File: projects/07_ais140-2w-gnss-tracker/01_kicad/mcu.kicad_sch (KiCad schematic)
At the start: 22 parts, among them J3 USB-C, J4 DEBUG TC2050, SW1 RESET, SW2 BOOT, U10 W25Q128JV, U8 ESP32-S3-WROOM-1-N8R2, U9 USBLC6-2SC6

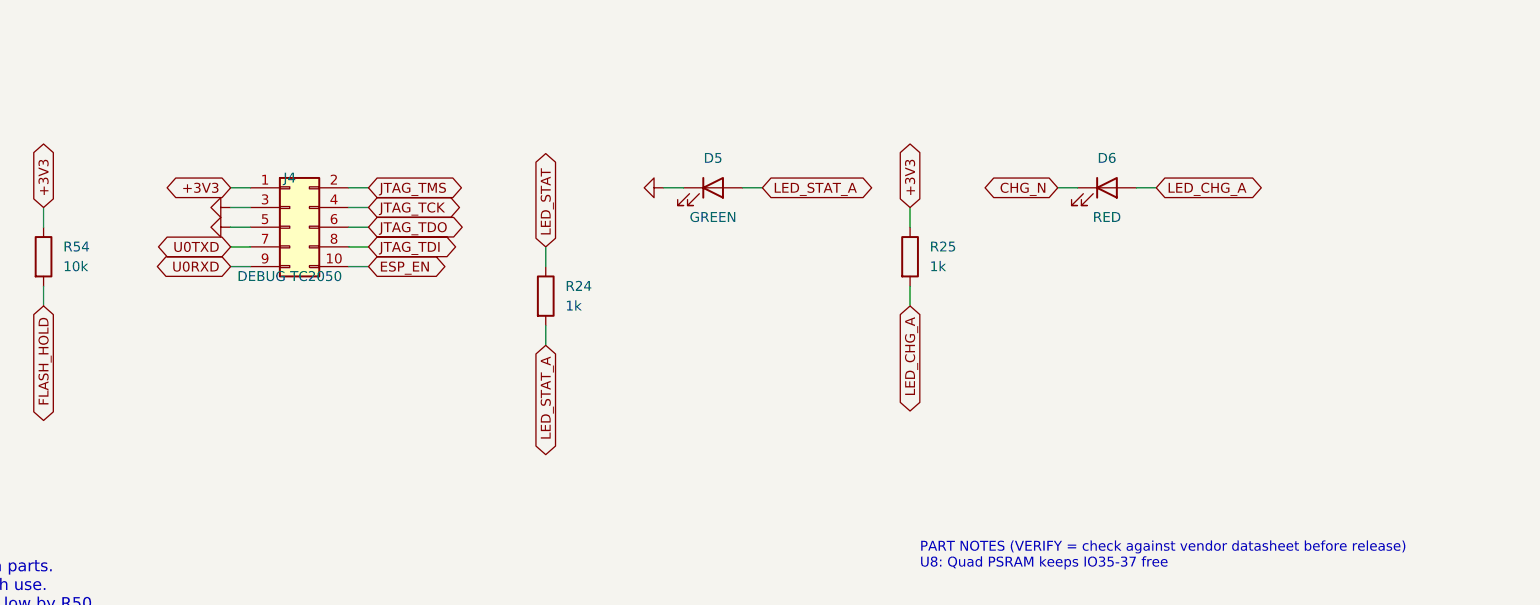
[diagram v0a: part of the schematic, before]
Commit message: Project 07: routed 4-layer PCB, fab outputs and 3D for the AIS-140 tracker
- 60x45 mm 4-layer board, double-sided assembly: KiCad DRC 0 errors / 0 unconnected,
  schematic parity clean, ERC clean
- Flow: anchors + greedy placer, GND/+3V3 fan-out, Freerouting 1.9, grid A* finisher
  with rip-up, RF via fences, edge/area stitching, island vias
- Gerbers + drill (zip), JLC BOM/CPL, engineering BOM, assembly PDFs, STEP + renders
  (envelope models for parts without a KiCad 3D model)
- Programming/JTAG via pogo test pads TP21-TP28 + native USB; R12 removed (TMR open)
- Design report updated with layout summary; DRC/ERC report added

Co-Authored-By: Claude Opus 5.5 <noreply@anthropic.com>
Claude-Session: https://claude.ai/code/session_01Hk6s8R6up8HYVQWXd3atVk
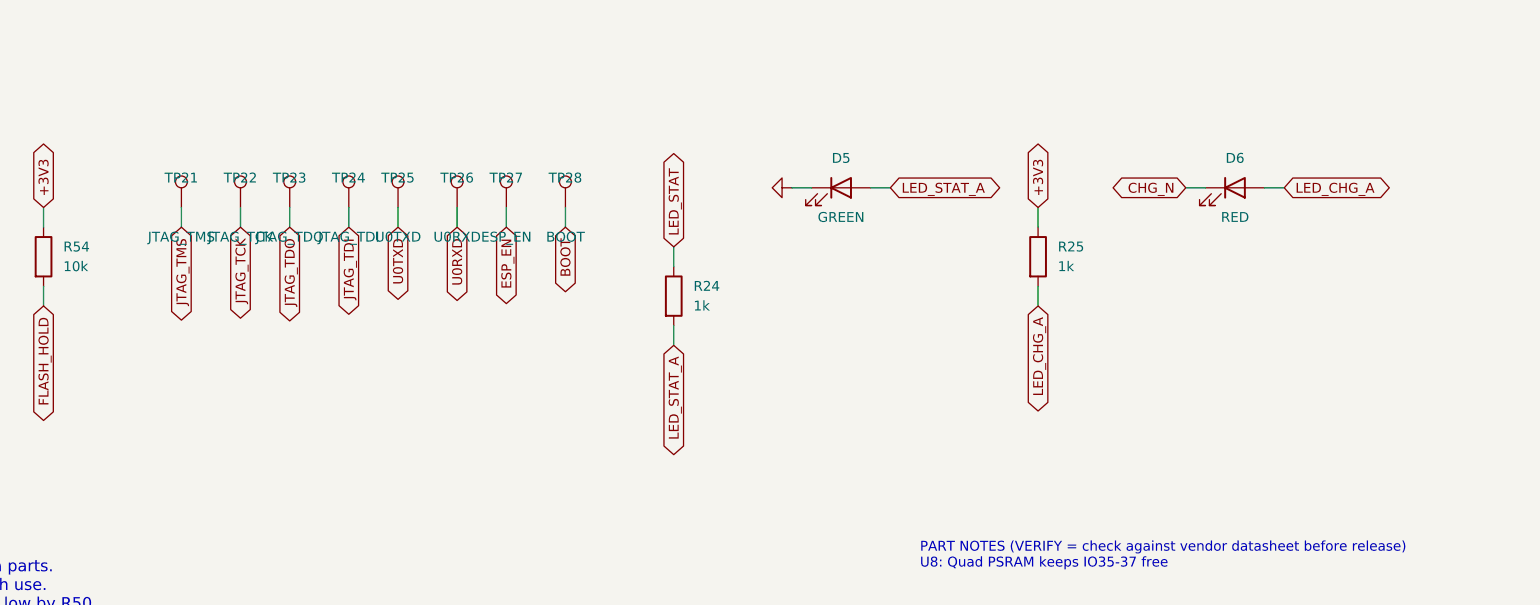
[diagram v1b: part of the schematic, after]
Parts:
- removed J4: DEBUG TC2050, Connector:Tag-Connect_TC2050-IDC-NL_2x05_P1.27mm_Vertical, symbol Connector_Generic:Conn_02x05_Odd_Even
- added TP21: JTAG_TMS, TestPoint:TestPoint_Pad_D1.0mm, symbol Connector:TestPoint
- added TP22: JTAG_TCK, TestPoint:TestPoint_Pad_D1.0mm, symbol Connector:TestPoint
- added TP23: JTAG_TDO, TestPoint:TestPoint_Pad_D1.0mm, symbol Connector:TestPoint
- added TP24: JTAG_TDI, TestPoint:TestPoint_Pad_D1.0mm, symbol Connector:TestPoint
- added TP25: U0TXD, TestPoint:TestPoint_Pad_D1.0mm, symbol Connector:TestPoint
- added TP26: U0RXD, TestPoint:TestPoint_Pad_D1.0mm, symbol Connector:TestPoint
- added TP27: ESP_EN, TestPoint:TestPoint_Pad_D1.0mm, symbol Connector:TestPoint
- added TP28: BOOT, TestPoint:TestPoint_Pad_D1.0mm, symbol Connector:TestPoint
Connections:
- net BOOT: now also TP28.1
- net ESP_EN: now also TP27.1
- net JTAG_TCK: now also TP22.1
- net JTAG_TDI: now also TP24.1
- net JTAG_TDO: now also TP23.1
- net JTAG_TMS: now also TP21.1
- net U0RXD: now also TP26.1
- net U0TXD: now also TP25.1
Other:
- moved on the sheet: D5, D6, R24, R25
